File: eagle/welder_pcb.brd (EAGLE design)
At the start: 38.1 x 40 mm, 12 parts, among them IC2 7805TV, Q1 16MHz

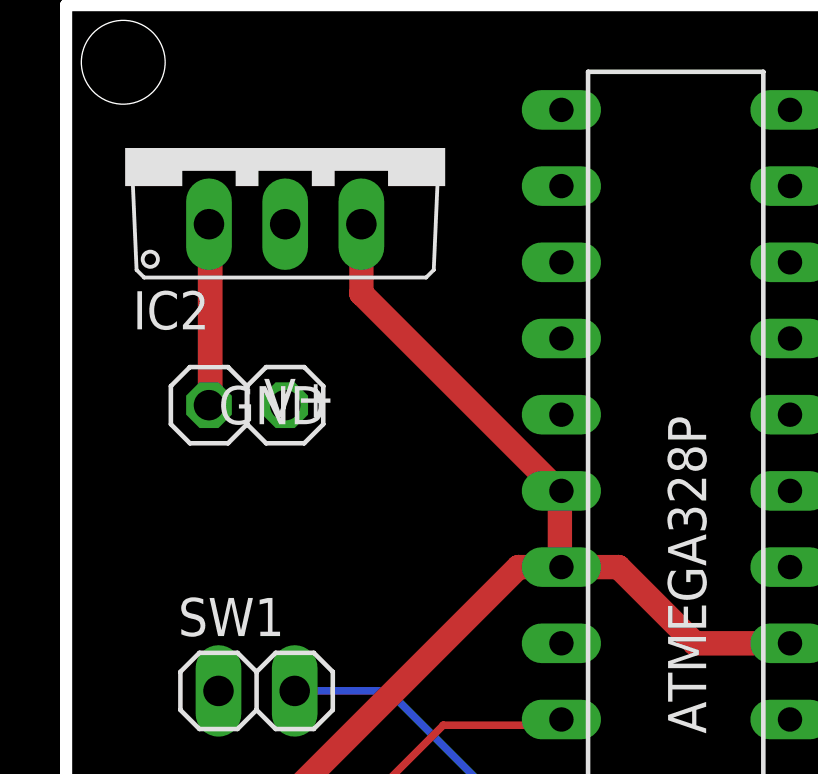
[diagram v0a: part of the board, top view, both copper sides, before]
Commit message: Add Relay Pins
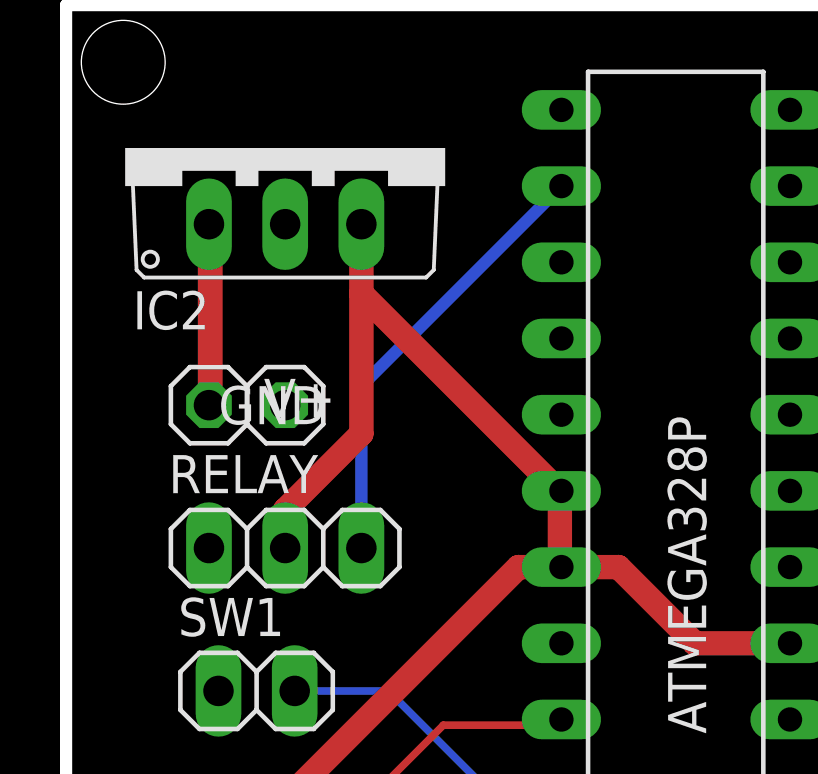
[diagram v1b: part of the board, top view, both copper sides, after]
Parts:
- added RELAY: (no value), pinhead:1X03
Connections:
- new net OC1B: ATMEGA328P.16, RELAY.3
- net +5V: now also RELAY.2
- net GND: now also RELAY.1
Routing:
- net OC1B: track 0.00 -> 14.8 mm
- net +5V: track 44.4 -> 54.0 mm
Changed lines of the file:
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@@
 <element name="TRIM" library="pinhead" library_urn="urn:adsk.eagle:library:325" package="1X03" package3d_urn="urn:adsk.eagle:package:22458/2" value="" x="7.62" y="11.1125"/>
 <element name="LCD" library="pinhead" library_urn="urn:adsk.eagle:library:325" package="1X03" package3d_urn="urn:adsk.eagle:package:22458/2" value="" x="7.62" y="5.3975"/>
+<element name="RELAY" library="pinhead" library_urn="urn:adsk.eagle:library:325" package="1X03" package3d_urn="urn:adsk.eagle:package:22458/2" value="" x="7.3025" y="21.9075"/>
 </elements>
 <signals>
@@
 <contactref element="TRIM" pad="3"/>
 <contactref element="LCD" pad="2"/>
+<contactref element="RELAY" pad="1"/>
 </signal>
 <signal name="N$1">
@@
 <wire x1="18.415" y1="21.2725" x2="20.955" y2="18.7325" width="0.8128" layer="1"/>
 <wire x1="20.955" y1="18.7325" x2="24.13" y2="18.7325" width="0.8128" layer="1"/>
+<contactref element="RELAY" pad="2"/>
+<wire x1="7.3025" y1="21.9075" x2="7.3025" y2="23.1775" width="0.8128" layer="1"/>
+<wire x1="7.3025" y1="23.1775" x2="9.8425" y2="25.7175" width="0.8128" layer="1"/>
+<wire x1="9.8425" y1="25.7175" x2="9.8425" y2="30.3911" width="0.8128" layer="1"/>
 </signal>
 <signal name="RESET">
@@
 <wire x1="28.3464" y1="3.2004" x2="28.575" y2="2.8575" width="0.254" layer="1"/>
 </signal>
+<signal name="OC1B">
+<contactref element="ATMEGA328P" pad="16"/>
+<contactref element="RELAY" pad="3"/>
+<wire x1="9.8425" y1="21.9075" x2="9.8425" y2="27.305" width="0.4064" layer="16"/>
+<wire x1="9.8425" y1="27.305" x2="16.51" y2="33.9725" width="0.4064" layer="16"/>
+</signal>
 </signals>
